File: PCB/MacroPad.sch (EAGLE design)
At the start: 42 parts, among them SW01 KEYSWITCH-PLAIN-MX-1U, SW02 KEYSWITCH-PLAIN-MX-1U, SW03 KEYSWITCH-PLAIN-MX-1U, SW04 KEYSWITCH-PLAIN-MX-1U, SW05 KEYSWITCH-PLAIN-MX-1U, SW06 KEYSWITCH-PLAIN-MX-1U, SW07 KEYSWITCH-PLAIN-MX-1U, SW08 KEYSWITCH-PLAIN-MX-1U, SW09 KEYSWITCH-PLAIN-MX-1U, SW10 KEYSWITCH-PLAIN-MX-1U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

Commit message: Use ATMEGA32U4-AU
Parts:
- U1: value ATMEGA32U4-AUR -> ATMEGA32U4-AU; device ATMEGA32U4-AUR:ATMEGA32U4-AUR -> ATMEGA32U4-AU:ATMEGA32U4-AU
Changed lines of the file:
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@@
 <part name="D10" library="adafruit" library_urn="urn:adsk.eagle:library:420" deviceset="DIODE" device="DO-1N4148" package3d_urn="urn:adsk.eagle:package:6240748/1"/>
 <part name="D11" library="adafruit" library_urn="urn:adsk.eagle:library:420" deviceset="DIODE" device="DO-1N4148" package3d_urn="urn:adsk.eagle:package:6240748/1"/>
-<part name="U1" library="ATMEGA32U4-AUR" deviceset="ATMEGA32U4-AUR" device=""/>
 <part name="SUPPLY9" library="supply2" library_urn="urn:adsk.eagle:library:372" deviceset="GND" device=""/>
 <part name="Y1" library="Controller" deviceset="CRYSTAL-4PIN" device="-3.2X5"/>
+<part name="U1" library="ATMEGA32U4-AU" deviceset="ATMEGA32U4-AU" device=""/>
 </parts>
 <sheets>
@@
 <attribute name="VALUE" x="247.65" y="10.16" size="1.27" layer="96" rot="R270"/>
 </instance>
-<instance part="U1" gate="A" x="152.4" y="76.2" smashed="yes">
-<attribute name="NAME" x="146.597359375" y="110.7105" size="2.08691875" layer="95" ratio="10" rot="SR0"/>
-<attribute name="VALUE" x="148.76276875" y="32.5533" size="2.085690625" layer="96" ratio="10" rot="SR0"/>
-</instance>
 <instance part="SUPPLY9" gate="GND" x="116.84" y="33.02" smashed="yes">
 <attribute name="VALUE" x="114.935" y="29.845" size="1.778" layer="96"/>
@@
 <attribute name="NAME" x="106.68" y="35.56" size="1.778" layer="95" font="vector" rot="R270" align="bottom-center"/>
 <attribute name="VALUE" x="109.22" y="35.56" size="1.778" layer="96" font="vector" rot="R270" align="bottom-center"/>
+</instance>
+<instance part="U1" gate="A" x="152.4" y="76.2" smashed="yes">
+<attribute name="NAME" x="146.602559375" y="110.6795" size="2.085040625" layer="95" ratio="10" rot="SR0"/>
+<attribute name="VALUE" x="148.76615" y="32.5938" size="2.08375" layer="96" ratio="10" rot="SR0"/>
 </instance>
 </instances>
@@
 <wire x1="101.6" y1="27.94" x2="104.14" y2="27.94" width="0.1524" layer="91"/>
 <pinref part="C2" gate="G$1" pin="2"/>
-<pinref part="U1" gate="A" pin="XTAL2"/>
 <wire x1="170.18" y1="43.18" x2="177.8" y2="43.18" width="0.1524" layer="91"/>
 <wire x1="177.8" y1="43.18" x2="177.8" y2="27.94" width="0.1524" layer="91"/>
 <wire x1="177.8" y1="27.94" x2="104.14" y2="27.94" width="0.1524" layer="91"/>
 <pinref part="Y1" gate="G$1" pin="2"/>
+<pinref part="U1" gate="A" pin="XTAL2"/>
 </segment>
 </net>
@@
 <junction x="104.14" y="43.18"/>
 <pinref part="C1" gate="G$1" pin="2"/>
-<pinref part="U1" gate="A" pin="XTAL1"/>
 <wire x1="104.14" y1="78.74" x2="134.62" y2="78.74" width="0.1524" layer="91"/>
 <pinref part="Y1" gate="G$1" pin="1"/>
+<pinref part="U1" gate="A" pin="XTAL1"/>
 </segment>
 </net>
@@
 <wire x1="101.6" y1="96.52" x2="127" y2="96.52" width="0.1524" layer="91"/>
 <wire x1="127" y1="96.52" x2="127" y2="99.06" width="0.1524" layer="91"/>
-<pinref part="U1" gate="A" pin="VCC_2"/>
 <wire x1="127" y1="99.06" x2="127" y2="101.6" width="0.1524" layer="91"/>
 <wire x1="127" y1="101.6" x2="127" y2="104.14" width="0.1524" layer="91"/>
 <wire x1="127" y1="104.14" x2="134.62" y2="104.14" width="0.1524" layer="91"/>
-<pinref part="U1" gate="A" pin="VCC"/>
 <wire x1="134.62" y1="101.6" x2="127" y2="101.6" width="0.1524" layer="91"/>
 <junction x="127" y="101.6"/>
-<pinref part="U1" gate="A" pin="AVCC_2"/>
 <wire x1="134.62" y1="96.52" x2="127" y2="96.52" width="0.1524" layer="91"/>
 <junction x="127" y="96.52"/>
-<pinref part="U1" gate="A" pin="AVCC"/>
 <wire x1="134.62" y1="93.98" x2="127" y2="93.98" width="0.1524" layer="91"/>
 <wire x1="127" y1="93.98" x2="127" y2="96.52" width="0.1524" layer="91"/>
-<pinref part="U1" gate="A" pin="VBUS"/>
 <wire x1="134.62" y1="73.66" x2="127" y2="73.66" width="0.1524" layer="91"/>
 <wire x1="127" y1="73.66" x2="127" y2="93.98" width="0.1524" layer="91"/>
 <junction x="127" y="93.98"/>
-<pinref part="U1" gate="A" pin="UVCC"/>
 <wire x1="134.62" y1="99.06" x2="127" y2="99.06" width="0.1524" layer="91"/>
 <junction x="127" y="99.06"/>
+<pinref part="U1" gate="A" pin="VCC_2"/>
+<pinref part="U1" gate="A" pin="VCC"/>
+<pinref part="U1" gate="A" pin="UVCC"/>
+<pinref part="U1" gate="A" pin="AVCC_2"/>
+<pinref part="U1" gate="A" pin="AVCC"/>
+<pinref part="U1" gate="A" pin="VBUS"/>
 </segment>
 </net>
@@
 <pinref part="RESET" gate="G$1" pin="2"/>
 <wire x1="96.52" y1="106.68" x2="99.06" y2="106.68" width="0.1524" layer="91"/>
-<pinref part="U1" gate="A" pin="~RESET"/>
 <wire x1="99.06" y1="106.68" x2="104.14" y2="106.68" width="0.1524" layer="91"/>
 <wire x1="104.14" y1="106.68" x2="104.14" y2="81.28" width="0.1524" layer="91"/>
@@
 <wire x1="99.06" y1="114.3" x2="99.06" y2="106.68" width="0.1524" layer="91"/>
 <junction x="99.06" y="106.68"/>
+<pinref part="U1" gate="A" pin="~RESET"/>
 </segment>
 </net>
@@
 <segment>
 <pinref part="C3" gate="G$1" pin="1"/>
-<pinref part="U1" gate="A" pin="UCAP"/>
 <wire x1="96.52" y1="76.2" x2="134.62" y2="76.2" width="0.1524" layer="91"/>
 <wire x1="93.98" y1="86.36" x2="96.52" y2="86.36" width="0.1524" layer="91"/>
 <wire x1="96.52" y1="86.36" x2="96.52" y2="76.2" width="0.1524" layer="91"/>
+<pinref part="U1" gate="A" pin="UCAP"/>
 </segment>
 </net>
@@
 <wire x1="99.06" y1="88.9" x2="99.06" y2="86.36" width="0.1524" layer="91"/>
 <pinref part="R3" gate="G$1" pin="2"/>
+<wire x1="134.62" y1="86.36" x2="99.06" y2="86.36" width="0.1524" layer="91"/>
 <pinref part="U1" gate="A" pin="D+"/>
-<wire x1="134.62" y1="86.36" x2="99.06" y2="86.36" width="0.1524" layer="91"/>
 </segment>
 </net>
@@
 <wire x1="210.82" y1="160.02" x2="243.84" y2="160.02" width="0.1524" layer="91"/>
 <wire x1="210.82" y1="81.28" x2="210.82" y2="160.02" width="0.1524" layer="91"/>
+<wire x1="170.18" y1="81.28" x2="210.82" y2="81.28" width="0.1524" layer="91"/>
 <pinref part="U1" gate="A" pin="PC6"/>
-<wire x1="170.18" y1="81.28" x2="210.82" y2="81.28" width="0.1524" layer="91"/>
 </segment>
 </net>
@@
 <pinref part="D3" gate="G$1" pin="C"/>
 <wire x1="274.32" y1="119.38" x2="274.32" y2="114.3" width="0.1524" layer="91"/>
+<wire x1="170.18" y1="63.5" x2="203.2" y2="63.5" width="0.1524" layer="91"/>
 <pinref part="U1" gate="A" pin="PD4"/>
-<wire x1="170.18" y1="63.5" x2="203.2" y2="63.5" width="0.1524" layer="91"/>
 </segment>
 </net>
@@
 <junction x="289.56" y="60.96"/>
 <wire x1="205.74" y1="165.1" x2="289.56" y2="165.1" width="0.1524" layer="91"/>
-<pinref part="U1" gate="A" pin="PB5"/>
 <wire x1="205.74" y1="91.44" x2="205.74" y2="165.1" width="0.1524" layer="91"/>
 <wire x1="170.18" y1="91.44" x2="205.74" y2="91.44" width="0.1524" layer="91"/>
+<pinref part="U1" gate="A" pin="PB5"/>
 </segment>
 </net>
@@
 <pinref part="D6" gate="G$1" pin="C"/>
 <wire x1="274.32" y1="81.28" x2="274.32" y2="76.2" width="0.1524" layer="91"/>
-<pinref part="U1" gate="A" pin="PD6"/>
 <wire x1="170.18" y1="58.42" x2="205.74" y2="58.42" width="0.1524" layer="91"/>
 <wire x1="205.74" y1="58.42" x2="205.74" y2="76.2" width="0.1524" layer="91"/>
+<pinref part="U1" gate="A" pin="PD6"/>
 </segment>
 </net>
@@
 <pinref part="D7" gate="G$1" pin="C"/>
 <wire x1="228.6" y1="43.18" x2="228.6" y2="38.1" width="0.1524" layer="91"/>
+<wire x1="170.18" y1="55.88" x2="205.74" y2="55.88" width="0.1524" layer="91"/>
 <pinref part="U1" gate="A" pin="PD7"/>
-<wire x1="170.18" y1="55.88" x2="205.74" y2="55.88" width="0.1524" layer="91"/>
 </segment>
 </net>
@@
 <pinref part="D12" gate="G$1" pin="C"/>
 <wire x1="274.32" y1="5.08" x2="274.32" y2="0" width="0.1524" layer="91"/>
-<pinref part="U1" gate="A" pin="PB4"/>
 <wire x1="170.18" y1="93.98" x2="200.66" y2="93.98" width="0.1524" layer="91"/>
 <wire x1="200.66" y1="93.98" x2="200.66" y2="0" width="0.1524" layer="91"/>
 <wire x1="200.66" y1="0" x2="228.6" y2="0" width="0.1524" layer="91"/>
+<pinref part="U1" gate="A" pin="PB4"/>
 </segment>
 </net>
@@
 <junction x="266.7" y="60.96"/>
 <wire x1="266.7" y1="162.56" x2="208.28" y2="162.56" width="0.1524" layer="91"/>
-<pinref part="U1" gate="A" pin="PB6"/>
 <wire x1="170.18" y1="88.9" x2="208.28" y2="88.9" width="0.1524" layer="91"/>
 <wire x1="208.28" y1="88.9" x2="208.28" y2="162.56" width="0.1524" layer="91"/>
+<pinref part="U1" gate="A" pin="PB6"/>
 </segment>
 </net>
@@
 <net name="N$4" class="0">
 <segment>
-<pinref part="U1" gate="A" pin="PE2"/>
 <wire x1="170.18" y1="50.8" x2="187.96" y2="50.8" width="0.1524" layer="91"/>
 <wire x1="187.96" y1="50.8" x2="187.96" y2="48.26" width="0.1524" layer="91"/>
 <pinref part="R2" gate="G$1" pin="2"/>
+<pinref part="U1" gate="A" pin="PE2"/>
 </segment>
 </net>
@@
 <pinref part="SUPPLY9" gate="GND" pin="GND"/>
 <wire x1="116.84" y1="35.56" x2="116.84" y2="45.72" width="0.1524" layer="91"/>
-<pinref part="U1" gate="A" pin="GND_3"/>
-<pinref part="U1" gate="A" pin="GND_2"/>
 <wire x1="134.62" y1="50.8" x2="129.54" y2="50.8" width="0.1524" layer="91"/>
 <wire x1="129.54" y1="50.8" x2="129.54" y2="48.26" width="0.1524" layer="91"/>
 <wire x1="129.54" y1="48.26" x2="134.62" y2="48.26" width="0.1524" layer="91"/>
 <junction x="129.54" y="48.26"/>
-<pinref part="U1" gate="A" pin="GND_4"/>
 <wire x1="134.62" y1="45.72" x2="129.54" y2="45.72" width="0.1524" layer="91"/>
 <wire x1="129.54" y1="45.72" x2="129.54" y2="48.26" width="0.1524" layer="91"/>
 <junction x="129.54" y="45.72"/>
-<pinref part="U1" gate="A" pin="GND"/>
 <wire x1="134.62" y1="43.18" x2="129.54" y2="43.18" width="0.1524" layer="91"/>
 <wire x1="129.54" y1="43.18" x2="129.54" y2="45.72" width="0.1524" layer="91"/>
 <junction x="129.54" y="43.18"/>
-<pinref part="U1" gate="A" pin="UGND"/>
 <wire x1="134.62" y1="40.64" x2="129.54" y2="40.64" width="0.1524" layer="91"/>
 <wire x1="129.54" y1="40.64" x2="129.54" y2="43.18" width="0.1524" layer="91"/>
 <wire x1="116.84" y1="45.72" x2="129.54" y2="45.72" width="0.1524" layer="91"/>
-</segment>
-</net>
+<pinref part="U1" gate="A" pin="GND_2"/>
+<pinref part="U1" gate="A" pin="GND_3"/>
+<pinref part="U1" gate="A" pin="GND_4"/>
+<pinref part="U1" gate="A" pin="GND"/>
+<pinref part="U1" gate="A" pin="UGND"/>
+</segment>
+</net>

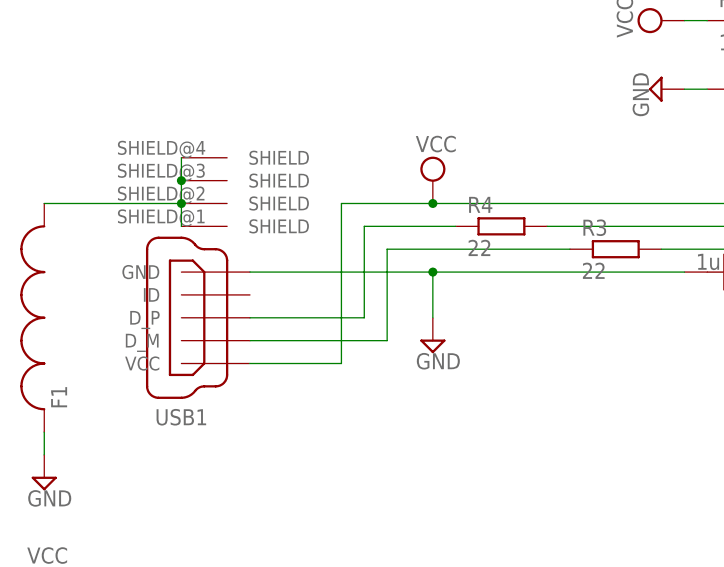
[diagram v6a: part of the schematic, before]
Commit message: Update PCB to correct D- and D+ mapping. Increment Date
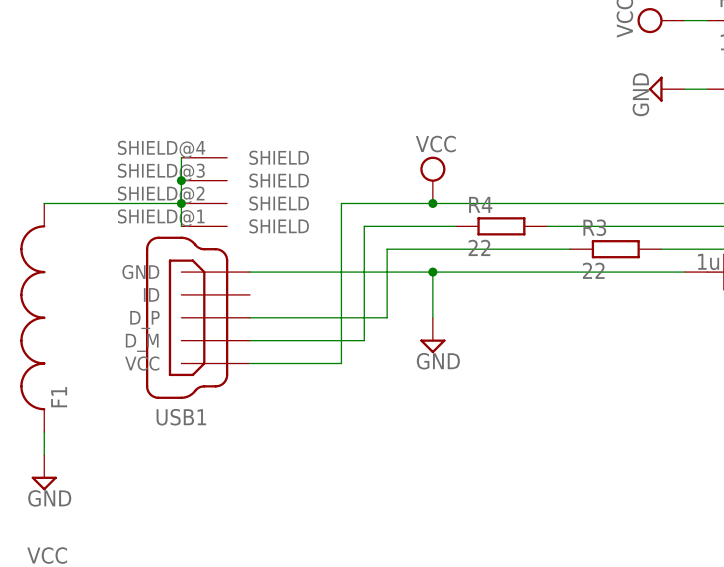
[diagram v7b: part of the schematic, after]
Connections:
- net N$5: now also USB1.D_M; no longer USB1.D_P
- net N$7: now also USB1.D_P; no longer USB1.D_M
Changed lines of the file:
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@@
 <net name="N$5" class="0">
 <segment>
-<pinref part="USB1" gate="G$1" pin="D_P"/>
-<wire x1="35.56" y1="81.28" x2="48.26" y2="81.28" width="0.1524" layer="91"/>
-<wire x1="48.26" y1="81.28" x2="48.26" y2="91.44" width="0.1524" layer="91"/>
+<wire x1="48.26" y1="78.74" x2="48.26" y2="91.44" width="0.1524" layer="91"/>
 <wire x1="48.26" y1="91.44" x2="58.42" y2="91.44" width="0.1524" layer="91"/>
 <pinref part="R4" gate="G$1" pin="1"/>
+<pinref part="USB1" gate="G$1" pin="D_M"/>
+<wire x1="35.56" y1="78.74" x2="48.26" y2="78.74" width="0.1524" layer="91"/>
 </segment>
 </net>
@@
 <net name="N$7" class="0">
 <segment>
-<pinref part="USB1" gate="G$1" pin="D_M"/>
-<wire x1="35.56" y1="78.74" x2="50.8" y2="78.74" width="0.1524" layer="91"/>
-<wire x1="50.8" y1="78.74" x2="50.8" y2="88.9" width="0.1524" layer="91"/>
 <wire x1="50.8" y1="88.9" x2="71.12" y2="88.9" width="0.1524" layer="91"/>
 <pinref part="R3" gate="G$1" pin="1"/>
+<wire x1="50.8" y1="88.9" x2="50.8" y2="81.28" width="0.1524" layer="91"/>
+<pinref part="USB1" gate="G$1" pin="D_P"/>
+<wire x1="50.8" y1="81.28" x2="35.56" y2="81.28" width="0.1524" layer="91"/>
 </segment>
 </net>
